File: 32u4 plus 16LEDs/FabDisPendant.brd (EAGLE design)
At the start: 59.2 x 41.6 mm, 57 parts, among them U2 MIC5219, U3 ATMEGA32U4, Y1 16MHz

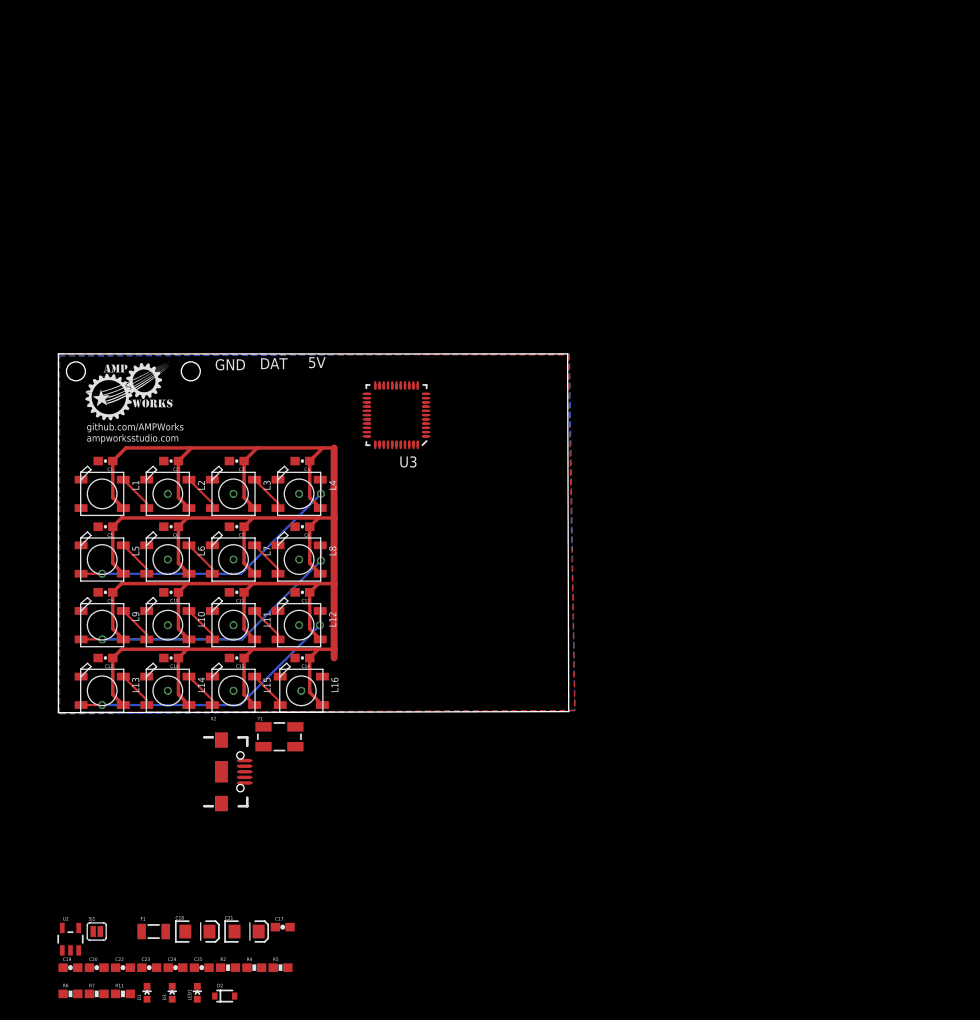
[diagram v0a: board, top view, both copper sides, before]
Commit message: Initial ATMega32u4 based pendant
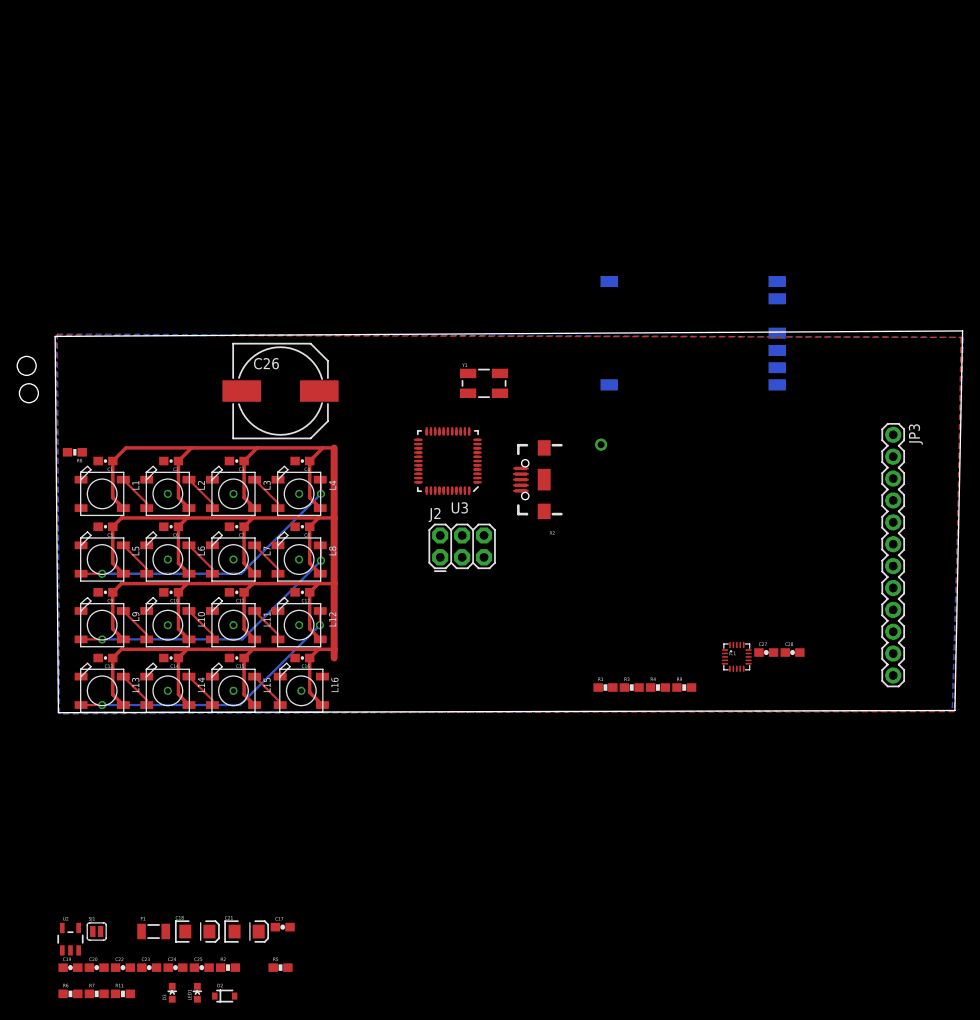
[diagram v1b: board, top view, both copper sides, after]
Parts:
- removed D1: Yellow, SparkFun:LED-0603
- added C26: 100uF, SparkFun-Capacitors:NIC_10X10.5_CAP
- added C27, C28: 0.1uF, SparkFun:0603-CAP
- added FRAME3: FRAME-LEDGER, SparkFun-Aesthetics:CREATIVE_COMMONS
- added IC1: MPR121, Testing:QFN-20-0.4MM-V2
- added J2: AVR_SPI_PRG_6PTH, SparkFun-Connectors:2X3
- added JP3: Electrodes, SparkFun:1X12
- added R1: 75k, SparkFun:0603-RES
- added R3, R9: 4.7k, SparkFun:0603-RES
- added R8: 220, SparkFun-Resistors:0603-RES
- added U$1: RFM12B_ANTENNA, LowPowerLab:RFM12B-ANTENNA
- added U$5: RFM69, LowPowerLab:RFM69W-MINPADS
- R4: value 330 -> 4.7k
- moved R4 57.0 mm to (69.6, 2.92)
- moved X2 50.5 mm to (56.4, 27.1), turned to 180 degrees
- moved Y1 47.4 mm to (49.4, 38.2)
- moved U3 8.01 mm to (45.2, 29.2)
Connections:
- removed net D10: L1.4-DIN, U3.30
- removed net D14: R4.1, U3.8
- removed net D2: U3.19
- removed net D3: U3.18
- removed net N$23: D1.C, R4.2
- removed net RXI: U3.20
- removed net TXO: U3.21
- new net 3.3V: C28.1, IC1.20, R3.2, R4.2, R9.2
- new net ADDR: IC1.4
- new net D10/LEDS: R8.1, U3.30
- new net ELE0: IC1.8, JP3.12
- new net ELE1: IC1.9, JP3.11
- new net ELE10: IC1.18, JP3.2
- new net ELE11: IC1.19, JP3.1
- new net ELE2: IC1.10, JP3.10
- new net ELE3: IC1.11, JP3.9
- new net ELE4: IC1.12, JP3.8
- new net ELE5: IC1.13, JP3.7
- new net ELE6: IC1.14, JP3.6
- new net ELE7: IC1.15, JP3.5
- new net ELE8: IC1.16, JP3.4
- new net ELE9: IC1.17, JP3.3
- new net MPRIRQ: IC1.1, R9.1, U3.21
- new net N$1: L1.4-DIN, R8.2
- new net N$25: U$1.P$1, U$5.ANA
- new net REXT: IC1.7, R1.2
- new net RMFIRQ: U$5.DIO0, U3.20
- new net SCL: IC1.2, R4.1, U3.18
- new net SDA: IC1.3, R3.1, U3.19
- new net SS: U$5.NSS, U3.8
- new net VREG: C27.1, IC1.5
- net GND: now also C26.-, C27.2, C28.2, IC1.6, J2.6, R1.1, U$5.GND
- net MISO: now also J2.1, U$5.MISO
- net MOSI: now also J2.4, U$5.MOSI
- net RESET: now also J2.5
- net SCK: now also J2.3, U$5.SCK
- net VCC: now also C26.+, J2.2, U$5.VDD; no longer D1.A
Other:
- board size 59.2 x 41.6 mm -> 105.3 x 44.3 mm
- board text removed: "5V"
- board text removed: "DAT"
- board text removed: "GND"
- board text removed: "ampworksstudio.com"
- board text removed: "github.com/AMPWorks"

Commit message: Routed MPR121 and USB
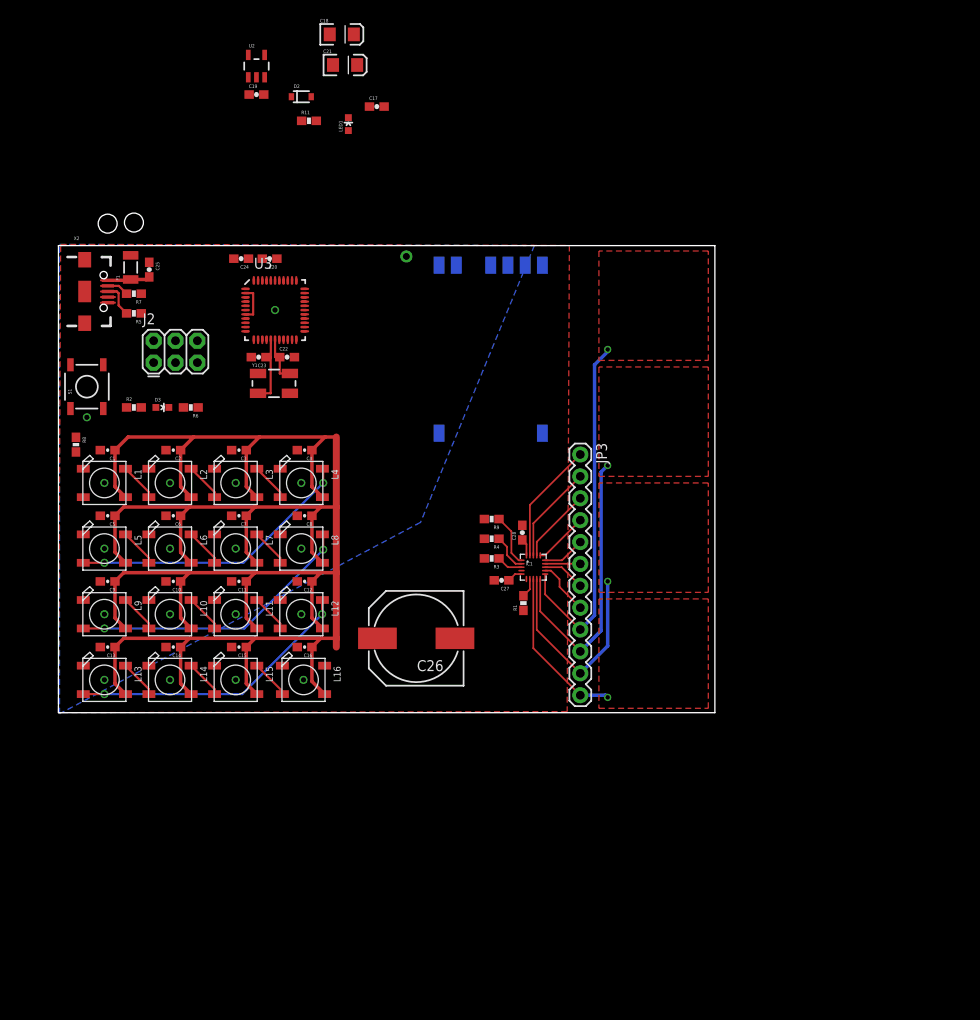
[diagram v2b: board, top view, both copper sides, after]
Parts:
- removed FRAME3: FRAME-LEDGER, SparkFun-Aesthetics:CREATIVE_COMMONS
- removed SJ1: Closed for 5V Board, SparkFun:SJ_2S
- added S1: Reset, SparkFun:TACTILE_SWITCH_SMD
- R8: device SparkFun-Resistors:0603-RES -> SparkFun-Resistors:0603-RES@1
- moved C18 105.5 mm to (32.9, 78.7)
- moved D2 104.8 mm to (28.2, 71.5)
- moved C19 103.6 mm to (23.0, 71.8)
- moved R11 103.6 mm to (29.1, 68.7)
- moved U2 103.6 mm to (23.0, 75.1)
- moved LED1 102.3 mm to (33.7, 68.3)
- moved C21 101.2 mm to (33.3, 75.2)
- moved C17 95.9 mm to (37.0, 70.4)
- moved C20 84.7 mm to (24.5, 52.7), turned to 180 degrees
- moved C24 82.6 mm to (21.2, 52.7), turned to 180 degrees
- moved R7 81.4 mm to (8.76, 48.6), turned to 180 degrees
- moved C25 81.3 mm to (10.5, 51.4), turned to 270 degrees
- moved R5 77.8 mm to (8.76, 46.4), turned to 180 degrees
- moved F1 77.1 mm to (8.38, 51.7), turned to 90 degrees
- moved C22 73.4 mm to (26.5, 41.3)
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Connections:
- net ELE0 renamed CAP0
- net ELE1 renamed CAP1
- net ELE10 renamed CAP10
- net ELE11 renamed CA011
- net ELE2 renamed CAP2
- net ELE3 renamed CAP3
- net ELE4 renamed CAP4
- net ELE5 renamed CAP5
- net ELE6 renamed CAP6
- net ELE7 renamed CAP7
- net ELE8 renamed CAP8
- net ELE9 renamed CAP9
- net UVCC renamed USBVCC
- removed net N$22: D2.2, F1.2, SJ1.1
- removed net VCC: C1.1, C10.1, C11.1, C12.1, C13.1, C14.1, C15.1, C16.1, C17.1, C18.A, C19.2, C2.1, C26.+, C3.1, C4.1, C5.1, C6.1, C7.1, C8.1, C9.1, D3.A, J2.2, L1.1-VDD, L10.1-VDD, L11.1-VDD, L12.1-VDD, L13.1-VDD, L14.1-VDD, L15.1-VDD, L16.1-VDD, L2.1-VDD, L3.1-VDD, L4.1-VDD, L5.1-VDD, L6.1-VDD, L7.1-VDD, L8.1-VDD, L9.1-VDD, R11.2, R2.2, SJ1.2, U$5.VDD, U2.5, U3.14, U3.24, U3.34, U3.44
- new net 5V: C1.1, C10.1, C11.1, C12.1, C13.1, C14.1, C15.1, C16.1, C17.1, C18.A, C19.2, C2.1, C26.+, C3.1, C4.1, C5.1, C6.1, C7.1, C8.1, C9.1, D2.2, D3.A, F1.2, J2.2, L1.1-VDD, L10.1-VDD, L11.1-VDD, L12.1-VDD, L13.1-VDD, L14.1-VDD, L15.1-VDD, L16.1-VDD, L2.1-VDD, L3.1-VDD, L4.1-VDD, L5.1-VDD, L6.1-VDD, L7.1-VDD, L8.1-VDD, L9.1-VDD, R11.2, R2.2, U2.5, U3.14, U3.24, U3.34, U3.44
- net 3.3V: now also U$5.VDD
- net GND: now also S1.1
- net RESET: now also S1.3
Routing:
- net VCC: track 244.0 -> 0.00 mm
- net 5V: track 0.00 -> 244.0 mm
- net CAP3: track 0.00 -> 42.0 mm, vias 0 -> 1
- net CAP2: track 0.00 -> 33.2 mm, vias 0 -> 1
- net CAP1: track 0.00 -> 25.0 mm, vias 0 -> 1
- net CAP0: track 0.00 -> 19.0 mm, vias 0 -> 1
- net CA011: track 0.00 -> 14.1 mm
- net CAP10: track 0.00 -> 11.4 mm
- net CAP9: track 0.00 -> 8.72 mm
- net N$17: track 0.00 -> 8.41 mm
- net USBVCC: track 0.00 -> 8.26 mm
- net CAP4: track 0.00 -> 6.39 mm
- net CAP8: track 0.00 -> 6.34 mm
- net MPRIRQ: track 0.00 -> 6.06 mm
- net N$18: track 0.00 -> 5.25 mm
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- added copper zone on layer 1, net CAP0
- added copper zone on layer 1, net CAP1
- added copper zone on layer 1, net CAP2
- added copper zone on layer 1, net CAP3
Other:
- board size 105.3 x 44.3 mm -> 76.2 x 54.2 mm
